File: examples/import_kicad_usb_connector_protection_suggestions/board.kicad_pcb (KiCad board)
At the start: 2.4 x 2.4 mm, 4 parts, among them J1 USB2_CONNECTOR

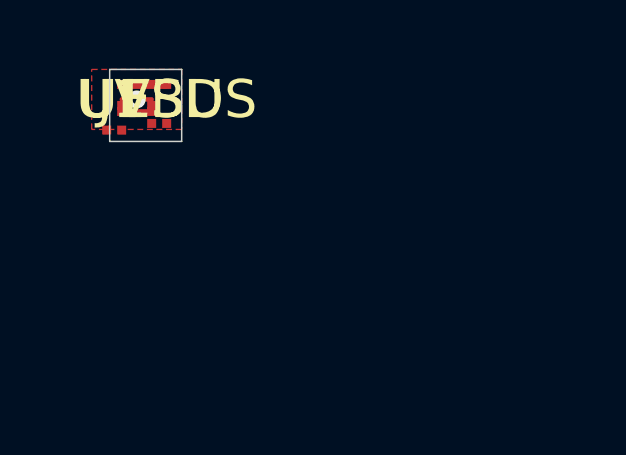
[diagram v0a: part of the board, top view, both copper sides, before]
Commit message: Import KiCad curved board outlines
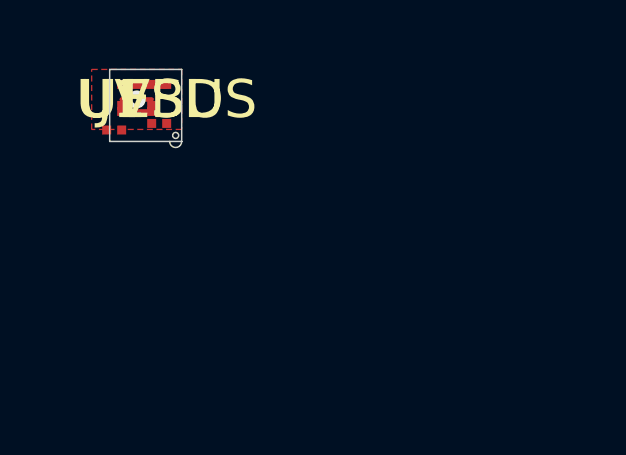
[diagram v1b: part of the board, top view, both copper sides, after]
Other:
- board size 2.4 x 2.4 mm -> 2.4 x 2.6 mm
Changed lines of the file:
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@@
   (gr_line (start 2.0 1.4) (end -0.4 1.4) (stroke (width 0.05) (type solid)) (layer "Edge.Cuts"))
   (gr_line (start -0.4 1.4) (end -0.4 -1.0) (stroke (width 0.05) (type solid)) (layer "Edge.Cuts"))
+  (gr_circle (center 1.8 1.2) (end 1.9 1.2) (stroke (width 0.05) (type solid)) (fill none) (layer "Edge.Cuts"))
+  (gr_arc (start 1.6 1.4) (mid 1.8 1.6) (end 2.0 1.4) (stroke (width 0.05) (type solid)) (layer "Edge.Cuts"))
   (footprint "Connector:USB2" (layer "F.Cu")
     (at 0 0 0)
